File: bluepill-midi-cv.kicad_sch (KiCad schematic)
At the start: 67 parts

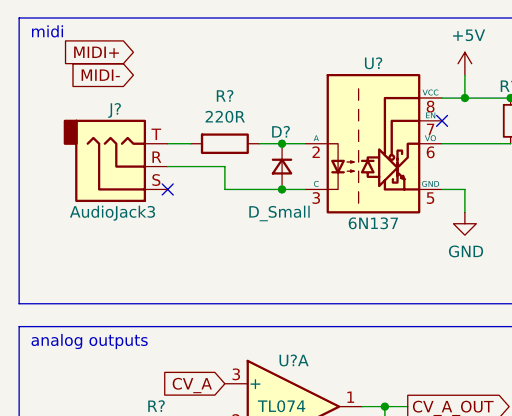
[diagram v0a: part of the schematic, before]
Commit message: connect midi-in to the connector board
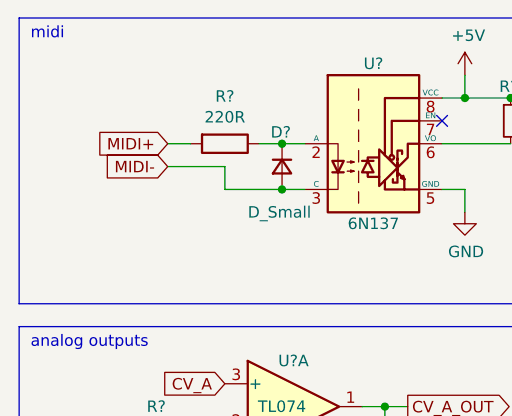
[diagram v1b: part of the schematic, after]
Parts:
- removed J?: AudioJack3, Connector_Audio:Jack_3.5mm_QingPu_WQP-PJ398SM_Vertical_CircularHoles, symbol Connector:AudioJack3
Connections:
- net MIDI+: now also R?.2
- net MIDI-: now also D?.2 (A), U?.3 (C)
- no-connect marks 43 -> 42
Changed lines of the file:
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@@
   (junction (at 170.18 34.29) (diameter 0) (color 0 0 0 0)
   )
-  (no_connect (at 30.48 33.02))
   (no_connect (at 246.38 92.71))
   (no_connect (at 228.6 133.35))
@@
     )
   )
-  (global_label "MIDI+" (shape input) (at 26.67 17.78 180) (fields_autoplaced)
-    (effects (font (size 1.27 1.27)) (justify right))
-    (property "Intersheet References" "${INTERSHEET_REFS}" (id 0) (at 18.8425 17.7006 0)
+  (global_label "MIDI+" (shape input) (at 30.48 27.94 180) (fields_autoplaced)
+    (effects (font (size 1.27 1.27)) (justify right))
+    (property "Intersheet References" "${INTERSHEET_REFS}" (id 0) (at 22.6525 27.8606 0)
       (effects (font (size 1.27 1.27)) (justify right) hide)
     )
@@
     )
   )
-  (global_label "MIDI-" (shape input) (at 26.67 20.32 180) (fields_autoplaced)
-    (effects (font (size 1.27 1.27)) (justify right))
-    (property "Intersheet References" "${INTERSHEET_REFS}" (id 0) (at 18.8425 20.2406 0)
+  (global_label "MIDI-" (shape input) (at 30.48 30.48 180) (fields_autoplaced)
+    (effects (font (size 1.27 1.27)) (justify right))
+    (property "Intersheet References" "${INTERSHEET_REFS}" (id 0) (at 22.6525 30.4006 0)
       (effects (font (size 1.27 1.27)) (justify right) hide)
     )
@@
     (pin "14")
   )
-  (symbol (lib_id "Connector:AudioJack3") (at 25.4 30.48 0) (mirror x) (unit 1)
-    (in_bom yes) (on_board yes)
-    (property "Reference" "J?" (id 0) (at 25.4 24.13 0)
-      (effects (font (size 1.27 1.27)) (justify right))
-    )
-    (property "Value" "AudioJack3" (id 1) (at 29.21 35.56 0)
-      (effects (font (size 1.27 1.27)) (justify right))
-    )
-    (property "Footprint" "Connector_Audio:Jack_3.5mm_QingPu_WQP-PJ398SM_Vertical_CircularHoles" (id 2) (at 25.4 30.48 0)
-      (effects (font (size 1.27 1.27)) hide)
-    )
-    (property "Datasheet" "~" (id 3) (at 25.4 30.48 0)
-      (effects (font (size 1.27 1.27)) hide)
-    )
-    (pin "R")
-    (pin "S")
-    (pin "T")
-  )
   (symbol (lib_id "Amplifier_Operational:TL074") (at 44.45 110.49 0) (unit 4)
     (in_bom yes) (on_board yes)
@@
       (reference "J?") (unit 1) (value "Conn_02x08_Odd_Even") (footprint "")
     )
-    (path "/697bada8-efdd-494e-ac19-64571d660035"
-      (reference "J?") (unit 1) (value "AudioJack3") (footprint "Connector_Audio:Jack_3.5mm_QingPu_WQP-PJ398SM_Vertical_CircularHoles")
-    )
     (path "/daa26a8e-18aa-46b3-b000-0b73d4ebda38"
